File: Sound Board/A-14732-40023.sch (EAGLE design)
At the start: 229 parts, among them P2 AUX IN, P3 AUX OUT, P4 ORKIN R/W, P5 VOLUME, P6 0.156", P7 0.156", Q1 MPS3646, U1 OKI6295, U10 26LS32A, U11 26LS31, U12 27C040-150, U13 27C040-150, U14 YAMAHA 2151, U15 TIL7524, U16 74LS374, U17 74LS174, U18 16L8, U19 74LS11, U2 2064, U20 74LS139, U21 74LS14, U22 74LS74, U23 74LS74, U24 26LS31, U25 26LS32A, U26 74LS04, U28 YAMAHA 3012, U29 LM324D, U3 27C040, U30 MC3340, U32 TL084D, U33 TL084D, U4 6809E, U5 74LS374DW, U6 26LS32A, U7 26LS31, U8 74LS138, U9 74LS74, Y1 3.5749MHz, Y2 8MHz

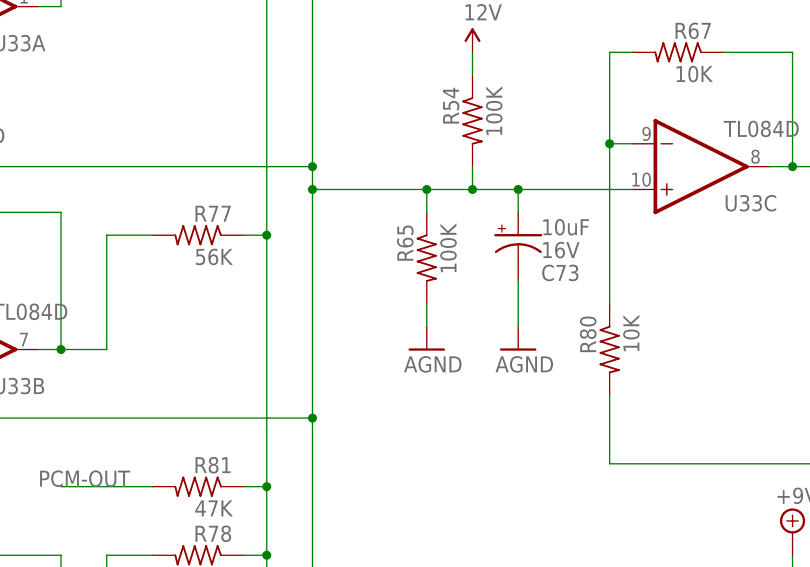
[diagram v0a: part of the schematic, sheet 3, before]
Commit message: R65 replaced with CR2 according to the official schematics
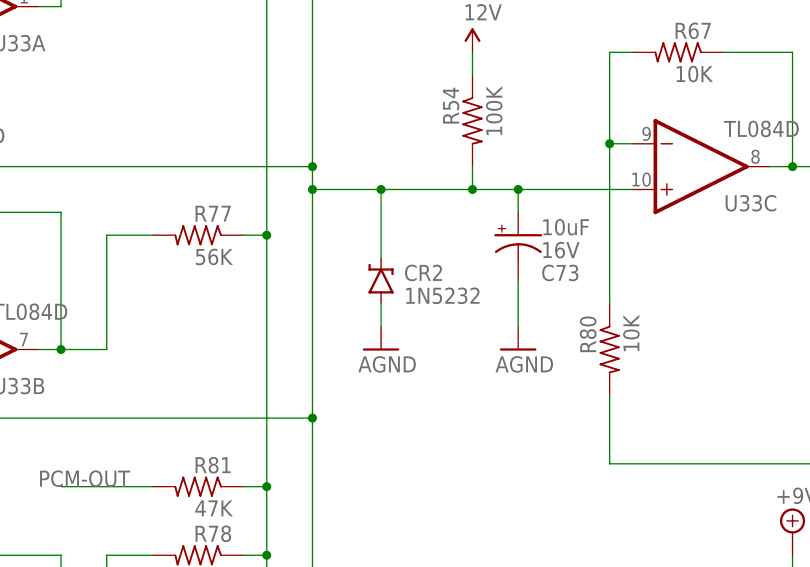
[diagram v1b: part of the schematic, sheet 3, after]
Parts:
- removed R65: 100K, resistor:R-US_R1206
- added CR2: 1N5232, A-14732-40023:1N5232
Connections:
- net AGND: now also CR2.A; no longer R65.2
- net N$76: now also CR2.C; no longer R65.1
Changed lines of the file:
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@@
 </part>
 <part name="R54" library="resistor" deviceset="R-US_" device="R1206" value="100K"/>
-<part name="R65" library="resistor" deviceset="R-US_" device="R1206" value="100K"/>
 <part name="U$28" library="SparkFun-Aesthetics" deviceset="AGND" device=""/>
 <part name="U$29" library="SparkFun-Aesthetics" deviceset="AGND" device=""/>
@@
 <part name="GND44" library="supply2" deviceset="GND" device=""/>
 <part name="U27" library="A-14732-40023" deviceset="MB3731" device=""/>
+<part name="CR2" library="A-14732-40023" deviceset="1N5232" device=""/>
 </parts>
 <sheets>
@@
 </instance>
 <instance part="R54" gate="G$1" x="139.7" y="190.5" rot="MR270"/>
-<instance part="R65" gate="G$1" x="134.62" y="175.26" rot="MR270"/>
-<instance part="U$28" gate="G$1" x="134.62" y="165.1"/>
+<instance part="U$28" gate="G$1" x="129.54" y="165.1"/>
 <instance part="U$29" gate="G$1" x="144.78" y="165.1"/>
 <instance part="R67" gate="G$1" x="162.56" y="198.12" rot="MR0"/>
@@
 <instance part="C65" gate="G$1" x="170.18" y="30.48" rot="MR180"/>
 <instance part="U27" gate="G$1" x="274.32" y="154.94"/>
+<instance part="CR2" gate="G$1" x="129.54" y="172.72"/>
 </instances>
 <busses>
@@
 </segment>
 <segment>
-<pinref part="R65" gate="G$1" pin="2"/>
 <pinref part="U$28" gate="G$1" pin="AGND"/>
-<wire x1="134.62" y1="170.18" x2="134.62" y2="167.64" width="0.1524" layer="91"/>
+<wire x1="129.54" y1="170.18" x2="129.54" y2="167.64" width="0.1524" layer="91"/>
+<pinref part="CR2" gate="G$1" pin="A"/>
 </segment>
 <segment>
@@
 <junction x="121.92" y="157.48"/>
 <pinref part="U33" gate="C" pin="+IN"/>
-<wire x1="121.92" y1="182.88" x2="134.62" y2="182.88" width="0.1524" layer="91"/>
+<wire x1="121.92" y1="182.88" x2="129.54" y2="182.88" width="0.1524" layer="91"/>
 <junction x="121.92" y="182.88"/>
 <pinref part="R54" gate="G$1" pin="2"/>
-<wire x1="134.62" y1="182.88" x2="139.7" y2="182.88" width="0.1524" layer="91"/>
+<wire x1="129.54" y1="182.88" x2="139.7" y2="182.88" width="0.1524" layer="91"/>
 <wire x1="139.7" y1="182.88" x2="144.78" y2="182.88" width="0.1524" layer="91"/>
 <wire x1="144.78" y1="182.88" x2="157.48" y2="182.88" width="0.1524" layer="91"/>
 <wire x1="139.7" y1="185.42" x2="139.7" y2="182.88" width="0.1524" layer="91"/>
 <junction x="139.7" y="182.88"/>
-<pinref part="R65" gate="G$1" pin="1"/>
-<wire x1="134.62" y1="182.88" x2="134.62" y2="180.34" width="0.1524" layer="91"/>
-<junction x="134.62" y="182.88"/>
+<wire x1="129.54" y1="182.88" x2="129.54" y2="175.26" width="0.1524" layer="91"/>
+<junction x="129.54" y="182.88"/>
 <pinref part="C73" gate="G$1" pin="+"/>
 <wire x1="144.78" y1="182.88" x2="144.78" y2="180.34" width="0.1524" layer="91"/>
 <junction x="144.78" y="182.88"/>
+<pinref part="CR2" gate="G$1" pin="C"/>
 </segment>
 </net>

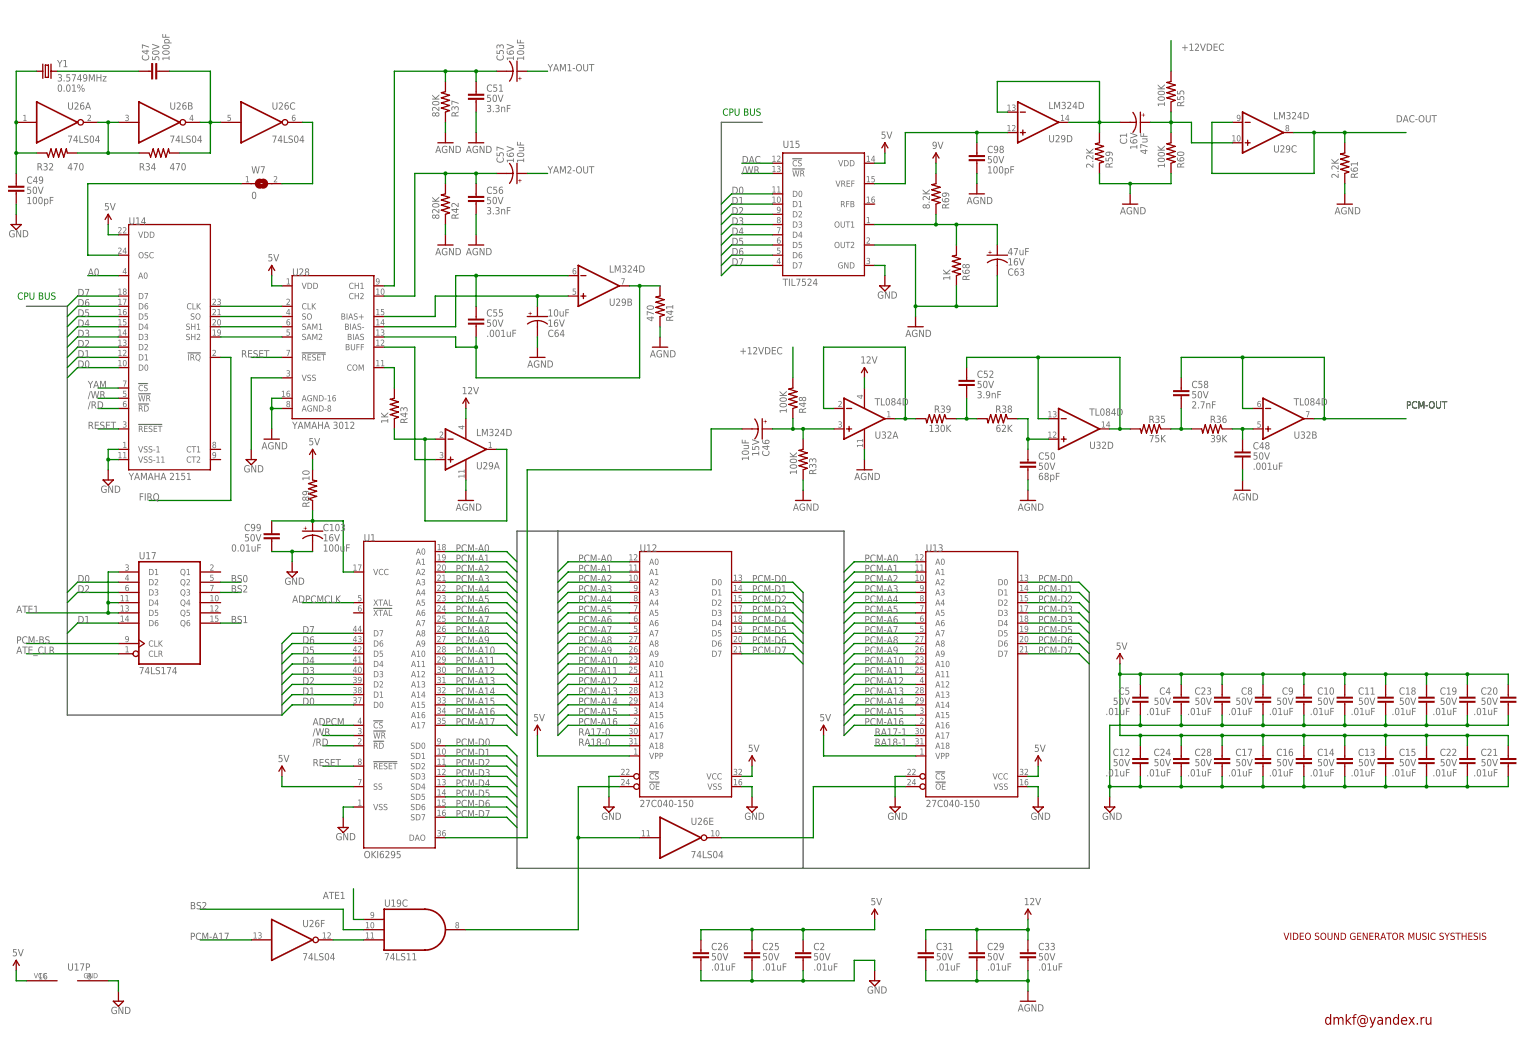
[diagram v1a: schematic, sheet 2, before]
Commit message: updated values, names, fixed some parts, added C104-C107 and R94-R96
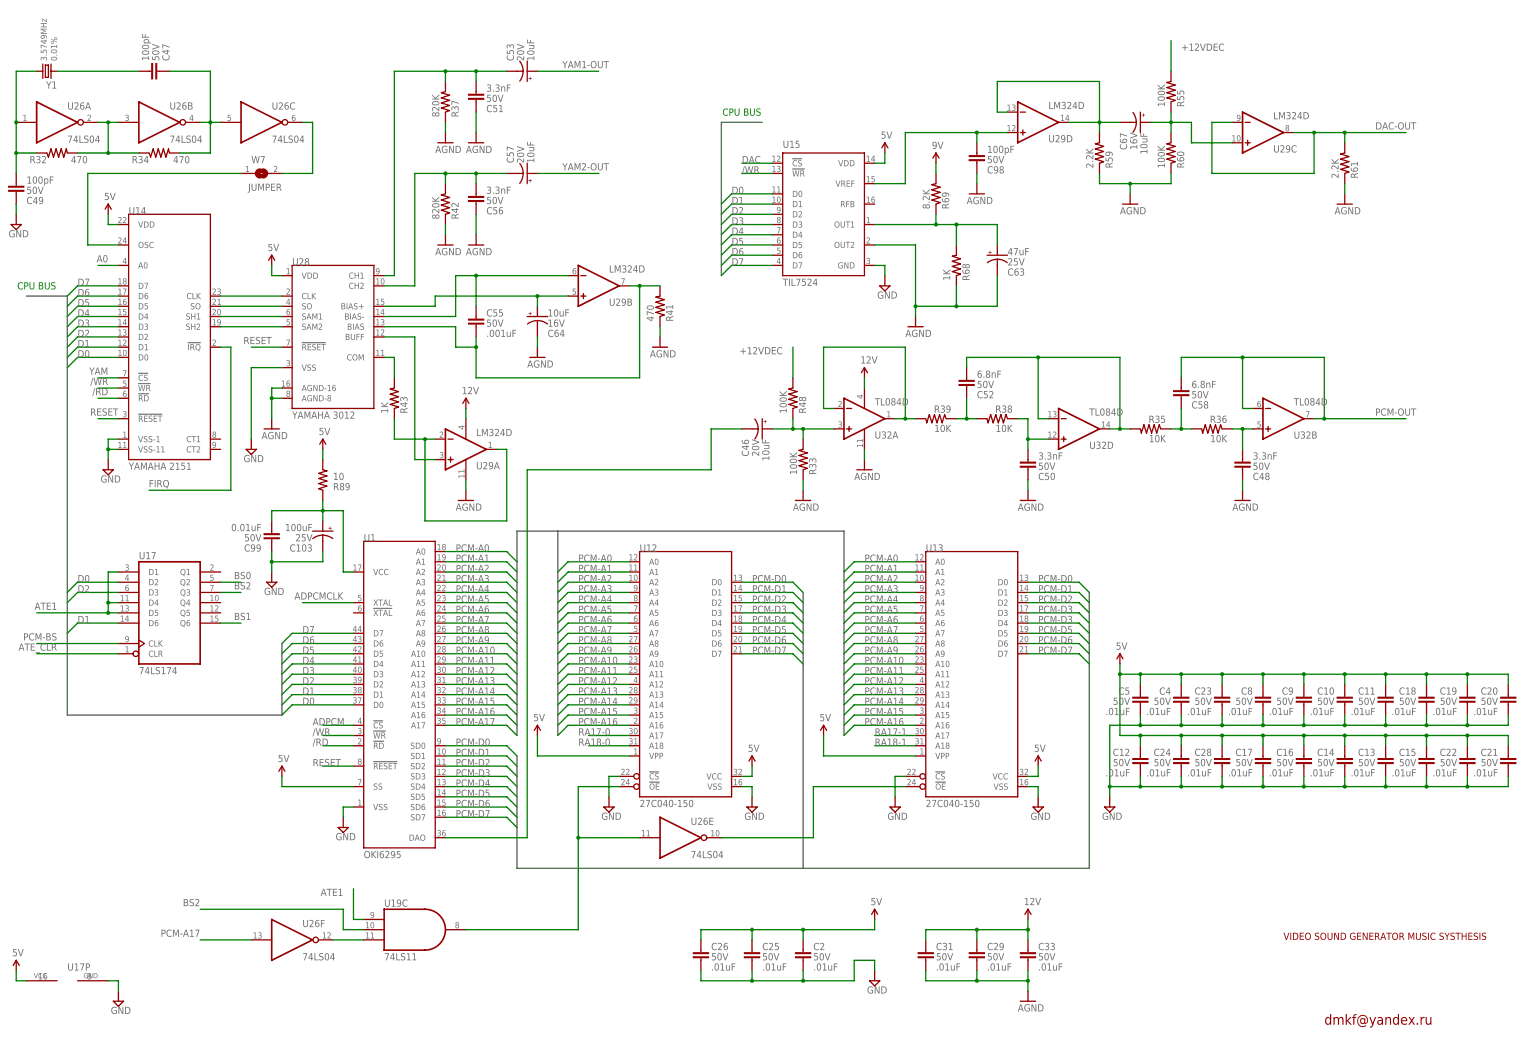
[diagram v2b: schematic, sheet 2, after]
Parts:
- added C104, C105, C106, C107: 100pF, SparkFun-Capacitors:1.0UF50V10%(1206)
- added R93, R94, R95, R96: 47, resistor:R-US_R1206
- C100: VOLTAGE (none) -> 20V
- C102, C53, C57, C73, C75, C81: VOLTAGE 16V -> 20V
- C103, C63, C66, C70, C85: VOLTAGE 16V -> 25V
- C46: VOLTAGE 15V -> 20V
- C48: value .001uF -> 3.3nF
- C50: value 68pF -> 3.3nF
- C52: value 3.9nF -> 6.8nF
- C58: value 2.7nF -> 6.8nF
- C67: value 47uF -> 10uF
- C68: VOLTAGE 25V -> 63V
- P2, P3, P4: PITCH (none) -> 0.100"
- R27: value 4.7K -> 150
- R28: value 4.7K -> 3.3K
- R35: value 75K -> 10K
- R36: value 39K -> 10K
- R38: value 62K -> 10K
- R39: value 130K -> 10K
- R54: value 100K -> 200
- R70: value 10K -> 47
- R71: value 68K -> 10K
- U31: value (none) -> MB3731
- W1, W2, W3, W4, W5, W6, W8: value JMP24G -> JUMPER
- W7: value 0 -> JUMPER
- renumbered C1 to C67, U27 to U31
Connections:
- removed net N$134: P1.16, R86.1, U25.INC
- new net N$101: P1.17, R93.2
- new net N$102: P1.18, R94.2
- new net N$97: P1.13, R96.2
- new net N$99: P1.16, R95.2
- new net SNDVIDRD: C105.2, R86.1, R95.1, U25.INC
- net 12V: now also U31.VCC
- net AGND: now also U31.GND_IN
- net B_VIDDAV: now also C104.2, R96.1; no longer P1.13
- net B_VIDRES: now also C106.1, R93.1; no longer P1.17
- net GND: now also C104.1, C105.1, C106.2, C107.2
- net N$103: now also U31.OUT(I)
- net N$91: now also U31.IN
- net N$92: now also U31.BYPASS
- net N$93: now also U31.FEEDBACK
- net N$94: now also U31.MUTE
- net N$96: now also U31.BS-I
- net SND_DAT8: now also C107.1, R94.1; no longer P1.18
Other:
- moved on the sheet: C103, C48, C53, C57, P1, P2, P5, R1, R4, R43, R89, U14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

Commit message: small fixes, WIP
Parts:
- C23, C28, C4, C5, C8: device SparkFun-Capacitors:1.0UF50V10%(1206) -> SparkFun-Passives:CAP0805
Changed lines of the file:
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@@
 <grid distance="0.1" unitdist="inch" unit="inch" style="lines" multiple="1" display="yes" altdistance="0.01" altunitdist="inch" altunit="inch"/>
 <layers>
-<layer number="1" name="Top" color="4" fill="1" visible="yes" active="no"/>
-<layer number="2" name="Route2" color="1" fill="3" visible="yes" active="no"/>
-<layer number="3" name="Route3" color="4" fill="3" visible="yes" active="no"/>
-<layer number="4" name="Route4" color="1" fill="4" visible="yes" active="no"/>
-<layer number="5" name="Route5" color="4" fill="4" visible="yes" active="no"/>
-<layer number="6" name="Route6" color="1" fill="8" visible="yes" active="no"/>
-<layer number="7" name="Route7" color="4" fill="8" visible="yes" active="no"/>
-<layer number="8" name="Route8" color="1" fill="2" visible="yes" active="no"/>
-<layer number="9" name="Route9" color="4" fill="2" visible="yes" active="no"/>
-<layer number="10" name="Route10" color="1" fill="7" visible="yes" active="no"/>
-<layer number="11" name="Route11" color="4" fill="7" visible="yes" active="no"/>
-<layer number="12" name="Route12" color="1" fill="5" visible="yes" active="no"/>
-<layer number="13" name="Route13" color="4" fill="5" visible="yes" active="no"/>
-<layer number="14" name="Route14" color="1" fill="6" visible="yes" active="no"/>
-<layer number="15" name="Route15" color="4" fill="6" visible="yes" active="no"/>
-<layer number="16" name="Bottom" color="1" fill="1" visible="yes" active="no"/>
-<layer number="17" name="Pads" color="2" fill="1" visible="yes" active="no"/>
-<layer number="18" name="Vias" color="2" fill="1" visible="yes" active="no"/>
-<layer number="19" name="Unrouted" color="6" fill="1" visible="yes" active="no"/>
-<layer number="20" name="Dimension" color="15" fill="1" visible="yes" active="no"/>
-<layer number="21" name="tPlace" color="7" fill="1" visible="yes" active="no"/>
-<layer number="22" name="bPlace" color="7" fill="1" visible="yes" active="no"/>
-<layer number="23" name="tOrigins" color="15" fill="1" visible="yes" active="no"/>
-<layer number="24" name="bOrigins" color="15" fill="1" visible="yes" active="no"/>
-<layer number="25" name="tNames" color="7" fill="1" visible="yes" active="no"/>
-<layer number="26" name="bNames" color="7" fill="1" visible="yes" active="no"/>
-<layer number="27" name="tValues" color="7" fill="1" visible="yes" active="no"/>
-<layer number="28" name="bValues" color="7" fill="1" visible="yes" active="no"/>
+<layer number="1" name="Top" color="4" fill="1" visible="no" active="no"/>
+<layer number="2" name="Route2" color="1" fill="3" visible="no" active="no"/>
+<layer number="3" name="Route3" color="4" fill="3" visible="no" active="no"/>
+<layer number="4" name="Route4" color="1" fill="4" visible="no" active="no"/>
+<layer number="5" name="Route5" color="4" fill="4" visible="no" active="no"/>
+<layer number="6" name="Route6" color="1" fill="8" visible="no" active="no"/>
+<layer number="7" name="Route7" color="4" fill="8" visible="no" active="no"/>
+<layer number="8" name="Route8" color="1" fill="2" visible="no" active="no"/>
+<layer number="9" name="Route9" color="4" fill="2" visible="no" active="no"/>
+<layer number="10" name="Route10" color="1" fill="7" visible="no" active="no"/>
+<layer number="11" name="Route11" color="4" fill="7" visible="no" active="no"/>
+<layer number="12" name="Route12" color="1" fill="5" visible="no" active="no"/>
+<layer number="13" name="Route13" color="4" fill="5" visible="no" active="no"/>
+<layer number="14" name="Route14" color="1" fill="6" visible="no" active="no"/>
+<layer number="15" name="Route15" color="4" fill="6" visible="no" active="no"/>
+<layer number="16" name="Bottom" color="1" fill="1" visible="no" active="no"/>
+<layer number="17" name="Pads" color="2" fill="1" visible="no" active="no"/>
+<layer number="18" name="Vias" color="2" fill="1" visible="no" active="no"/>
+<layer number="19" name="Unrouted" color="6" fill="1" visible="no" active="no"/>
+<layer number="20" name="Dimension" color="15" fill="1" visible="no" active="no"/>
+<layer number="21" name="tPlace" color="7" fill="1" visible="no" active="no"/>
+<layer number="22" name="bPlace" color="7" fill="1" visible="no" active="no"/>
+<layer number="23" name="tOrigins" color="15" fill="1" visible="no" active="no"/>
+<layer number="24" name="bOrigins" color="15" fill="1" visible="no" active="no"/>
+<layer number="25" name="tNames" color="7" fill="1" visible="no" active="no"/>
+<layer number="26" name="bNames" color="7" fill="1" visible="no" active="no"/>
+<layer number="27" name="tValues" color="7" fill="1" visible="no" active="no"/>
+<layer number="28" name="bValues" color="7" fill="1" visible="no" active="no"/>
 <layer number="29" name="tStop" color="7" fill="3" visible="no" active="no"/>
 <layer number="30" name="bStop" color="7" fill="6" visible="no" active="no"/>
@@
 <layer number="35" name="tGlue" color="7" fill="4" visible="no" active="no"/>
 <layer number="36" name="bGlue" color="7" fill="5" visible="no" active="no"/>
-<layer number="37" name="tTest" color="7" fill="1" visible="yes" active="no"/>
-<layer number="38" name="bTest" color="7" fill="1" visible="yes" active="no"/>
+<layer number="37" name="tTest" color="7" fill="1" visible="no" active="no"/>
+<layer number="38" name="bTest" color="7" fill="1" visible="no" active="no"/>
 <layer number="39" name="tKeepout" color="4" fill="11" visible="no" active="no"/>
 <layer number="40" name="bKeepout" color="1" fill="11" visible="no" active="no"/>
@@
 <layer number="44" name="Drills" color="7" fill="1" visible="no" active="no"/>
 <layer number="45" name="Holes" color="7" fill="1" visible="no" active="no"/>
-<layer number="46" name="Milling" color="3" fill="1" visible="yes" active="no"/>
-<layer number="47" name="Measures" color="7" fill="1" visible="yes" active="no"/>
-<layer number="48" name="Document" color="7" fill="1" visible="yes" active="no"/>
-<layer number="49" name="Reference" color="7" fill="1" visible="yes" active="no"/>
-<layer number="50" name="dxf" color="7" fill="1" visible="yes" active="no"/>
-<layer number="51" name="tDocu" color="7" fill="1" visible="yes" active="no"/>
-<layer number="52" name="bDocu" color="7" fill="1" visible="yes" active="no"/>
-<layer number="53" name="tGND_GNDA" color="7" fill="9" visible="yes" active="no"/>
-<layer number="54" name="bGND_GNDA" color="1" fill="9" visible="yes" active="no"/>
-<layer number="56" name="wert" color="7" fill="1" visible="yes" active="no"/>
-<layer number="57" name="tCAD" color="7" fill="1" visible="yes" active="no"/>
-<layer number="59" name="tCarbon" color="7" fill="1" visible="yes" active="no"/>
-<layer number="60" name="bCarbon" color="7" fill="1" visible="yes" active="no"/>
+<layer number="46" name="Milling" color="3" fill="1" visible="no" active="no"/>
+<layer number="47" name="Measures" color="7" fill="1" visible="no" active="no"/>
+<layer number="48" name="Document" color="7" fill="1" visible="no" active="no"/>
+<layer number="49" name="Reference" color="7" fill="1" visible="no" active="no"/>
+<layer number="50" name="dxf" color="7" fill="1" visible="no" active="no"/>
+<layer number="51" name="tDocu" color="7" fill="1" visible="no" active="no"/>
+<layer number="52" name="bDocu" color="7" fill="1" visible="no" active="no"/>
+<layer number="53" name="tGND_GNDA" color="7" fill="9" visible="no" active="no"/>
+<layer number="54" name="bGND_GNDA" color="1" fill="9" visible="no" active="no"/>
+<layer number="56" name="wert" color="7" fill="1" visible="no" active="no"/>
+<layer number="57" name="tCAD" color="7" fill="1" visible="no" active="no"/>
+<layer number="59" name="tCarbon" color="7" fill="1" visible="no" active="no"/>
+<layer number="60" name="bCarbon" color="7" fill="1" visible="no" active="no"/>
 <layer number="90" name="Modules" color="5" fill="1" visible="yes" active="yes"/>
 <layer number="91" name="Nets" color="2" fill="1" visible="yes" active="yes"/>
@@
 <attribute name="VOLTAGE" value="50V"/>
 </part>
-<part name="C8" library="SparkFun-Capacitors" deviceset="1.0UF50V10%(1206)" device="" value=".01uF">
-<attribute name="VOLTAGE" value="50V"/>
-</part>
-<part name="C23" library="SparkFun-Capacitors" deviceset="1.0UF50V10%(1206)" device="" value=".01uF">
-<attribute name="VOLTAGE" value="50V"/>
-</part>
-<part name="C4" library="SparkFun-Capacitors" deviceset="1.0UF50V10%(1206)" device="" value=".01uF">
-<attribute name="VOLTAGE" value="50V"/>
-</part>
-<part name="C5" library="SparkFun-Capacitors" deviceset="1.0UF50V10%(1206)" device="" value=".01uF">
+<part name="C8" library="SparkFun-Passives" deviceset="CAP" device="0805" value=".01uF">
+<attribute name="VOLTAGE" value="50V"/>
+</part>
+<part name="C23" library="SparkFun-Passives" deviceset="CAP" device="0805" value=".01uF">
+<attribute name="VOLTAGE" value="50V"/>
+</part>
+<part name="C4" library="SparkFun-Passives" deviceset="CAP" device="0805" value=".01uF">
+<attribute name="VOLTAGE" value="50V"/>
+</part>
+<part name="C5" library="SparkFun-Passives" deviceset="CAP" device="0805" value=".01uF">
 <attribute name="VOLTAGE" value="50V"/>
 </part>
@@
 <attribute name="VOLTAGE" value="50V"/>
 </part>
-<part name="C28" library="SparkFun-Capacitors" deviceset="1.0UF50V10%(1206)" device="" value=".01uF">
-<attribute name="VOLTAGE" value="50V"/>
-</part>
+<part name="C28" library="SparkFun-Passives" deviceset="CAP" device="0805" value=".01uF">
+<attribute name="VOLTAGE" value="50V"/>
+</part>
